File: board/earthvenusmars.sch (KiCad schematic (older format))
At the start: 31 parts, among them J1 Conn_01x05_Female, SW1 SW_SPST, SW2 SW_SPST, U1 ATSAMD21G18A-AU, U2 MIC5504-3.3YM5, Y1 32768Hz

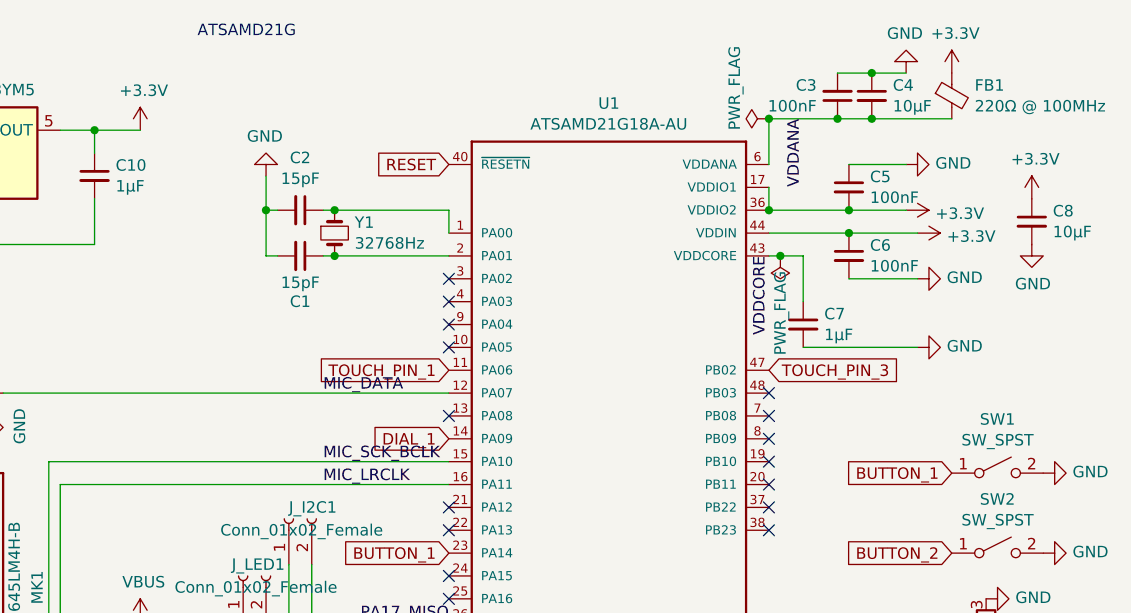
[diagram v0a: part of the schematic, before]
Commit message: add a thermistor that I can use to manage thermals
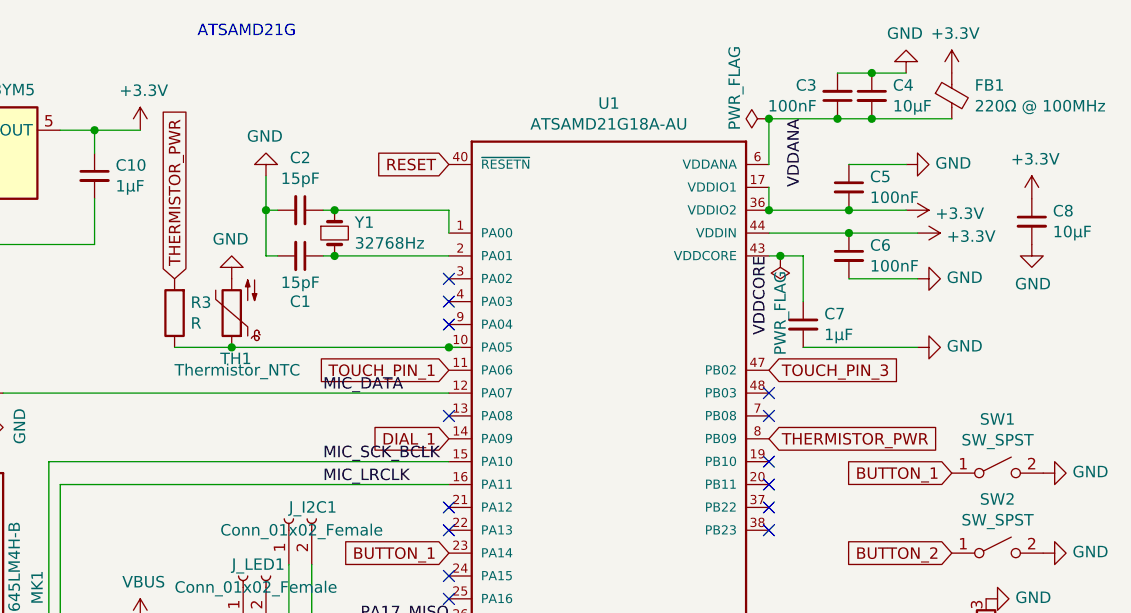
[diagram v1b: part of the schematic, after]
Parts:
- added R3: R, Resistor_SMD:R_0603_1608Metric, symbol Device:R
- added TH1: Thermistor_NTC, Resistor_SMD:R_0603_1608Metric, symbol Device:Thermistor_NTC
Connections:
- net GND: now also TH1.2
- net at U1.10 (PA05): now also R3.1, TH1.1
- net THERMISTOR_PWR: now reaches U1.8 (PB09)
- net THERMISTOR_PWR: now also R3.2
- no-connect marks 21 -> 19
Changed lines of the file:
@@
 NoConn ~ 5350 2350
 NoConn ~ 5350 2450
-NoConn ~ 5350 2550
 NoConn ~ 5350 2650
 NoConn ~ 5350 2750
@@
 Text GLabel 5350 2250 2    50   Input ~ 0
 TOUCH_PIN_3
-NoConn ~ 3950 2150
 $Comp
 L Connector:Conn_01x02_Female J_LED1
@@
 Wire Wire Line
 	2600 4800 3400 4800
+$Comp
+L Device:Thermistor_NTC TH1
+U 1 1 60C6FD5E
+P 3000 2000
+F 0 "TH1" H 3050 2200 50  0000 R CNN
+F 1 "Thermistor_NTC" H 3250 2250 50  0000 R CNN
+F 2 "Resistor_SMD:R_0603_1608Metric" H 3000 2050 50  0001 C CNN
+F 3 "~" H 3000 2050 50  0001 C CNN
+F 4 "ERTJ1VG103GA" H 3000 2000 50  0001 C CNN "Designation"
+	1    3000 2000
+	-1   0    0    1
+$EndComp
+$Comp
+L Device:R R3
+U 1 1 60C7ADC4
+P 2750 2000
+F 0 "R3" H 2680 1954 50  0000 R CNN
+F 1 "R" H 2680 2045 50  0000 R CNN
+F 2 "Resistor_SMD:R_0603_1608Metric" V 2680 2000 50  0001 C CNN
+F 3 "~" H 2750 2000 50  0001 C CNN
+	1    2750 2000
+	-1   0    0    1
+$EndComp
+Text GLabel 5350 2550 2    50   Input ~ 0
+THERMISTOR_PWR
+Text GLabel 2750 1850 1    50   Input ~ 0
+THERMISTOR_PWR
+Wire Wire Line
+	3000 2150 3950 2150
+$Comp
+L power:GND #PWR?
+U 1 1 60C9B9A5
+P 3000 1850
+F 0 "#PWR?" H 3000 1600 50  0001 C CNN
+F 1 "GND" H 3005 1677 50  0000 C CNN
+F 2 "" H 3000 1850 50  0001 C CNN
+F 3 "" H 3000 1850 50  0001 C CNN
+	1    3000 1850
+	-1   0    0    1
+$EndComp
+Connection ~ 3950 2150
+Wire Wire Line
+	3950 2150 4000 2150
+Connection ~ 3000 2150
+Wire Wire Line
+	2750 2150 3000 2150
 $EndSCHEMATC

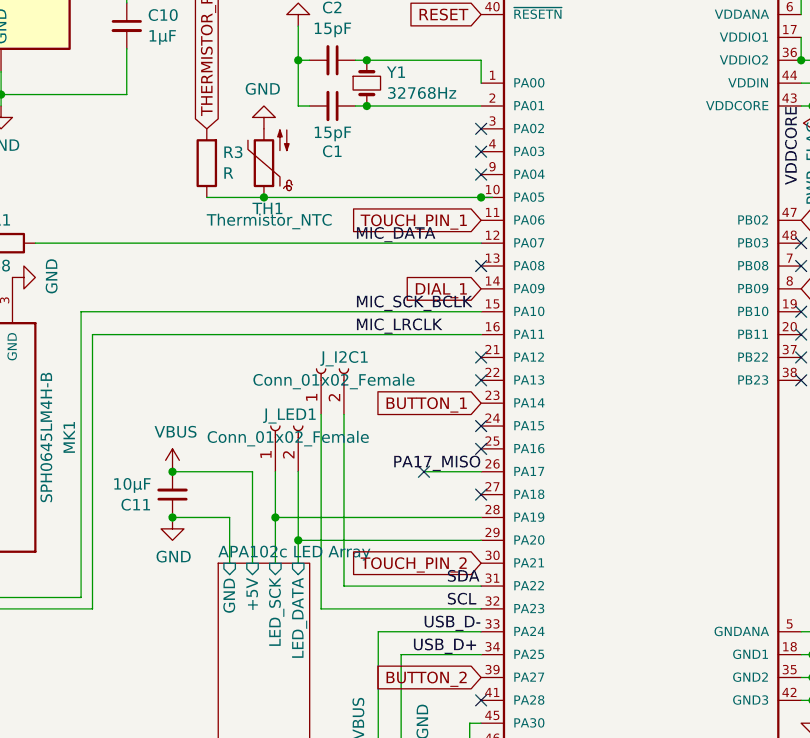
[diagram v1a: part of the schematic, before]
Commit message: move touch pin 2 because AdaFruit_FreeTouch only supports PA02 thru PA07 for self-capacitance; run power to mic and VDDANA on the far side of the VDDIO capacitor to save a via, I think this'll be fine; scoot a bunch of stuff around to optimize ground plane
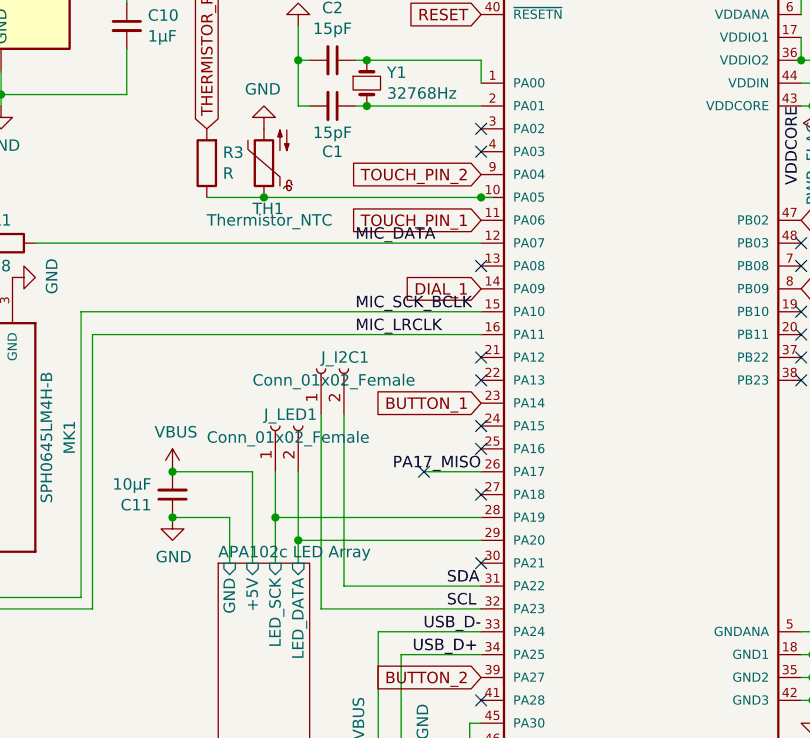
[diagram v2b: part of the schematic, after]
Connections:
- net TOUCH_PIN_2: now also U1.9 (PA04); no longer U1.30 (PA21)
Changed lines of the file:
@@
 NoConn ~ 3950 2950
 NoConn ~ 3950 2850
-NoConn ~ 3950 2050
+NoConn ~ 3950 2450
 NoConn ~ 3950 1950
 NoConn ~ 3950 1850
@@
 Text GLabel 3950 2250 0    50   Input ~ 0
 TOUCH_PIN_1
-NoConn ~ 3950 2450
-Text GLabel 3950 3750 0    50   Input ~ 0
+NoConn ~ 3950 3750
+Text GLabel 3950 2050 0    50   Input ~ 0
 TOUCH_PIN_2
 Text GLabel 6300 3950 0    50   Input ~ 0
@@
 	3000 2150 3950 2150
 $Comp
-L power:GND #PWR?
+L power:GND #PWR0137
 U 1 1 60C9B9A5
 P 3000 1850
-F 0 "#PWR?" H 3000 1600 50  0001 C CNN
+F 0 "#PWR0137" H 3000 1600 50  0001 C CNN
 F 1 "GND" H 3005 1677 50  0000 C CNN
 F 2 "" H 3000 1850 50  0001 C CNN

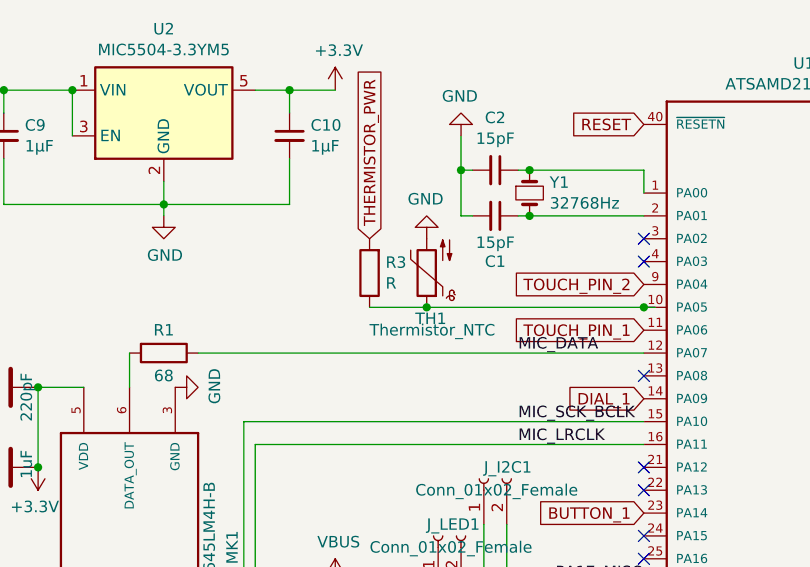
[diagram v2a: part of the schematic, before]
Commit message: thermistor series resister marked as 10k
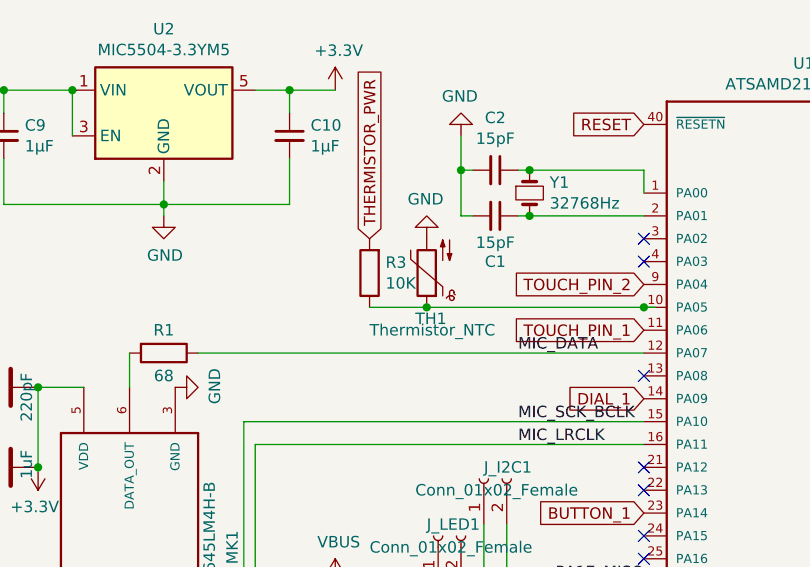
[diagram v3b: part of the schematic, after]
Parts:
- R3: value R -> 10K
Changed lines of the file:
@@
 P 2750 2000
 F 0 "R3" H 2680 1954 50  0000 R CNN
-F 1 "R" H 2680 2045 50  0000 R CNN
+F 1 "10K" H 2680 2045 50  0000 R CNN
 F 2 "Resistor_SMD:R_0603_1608Metric" V 2680 2000 50  0001 C CNN
 F 3 "~" H 2750 2000 50  0001 C CNN

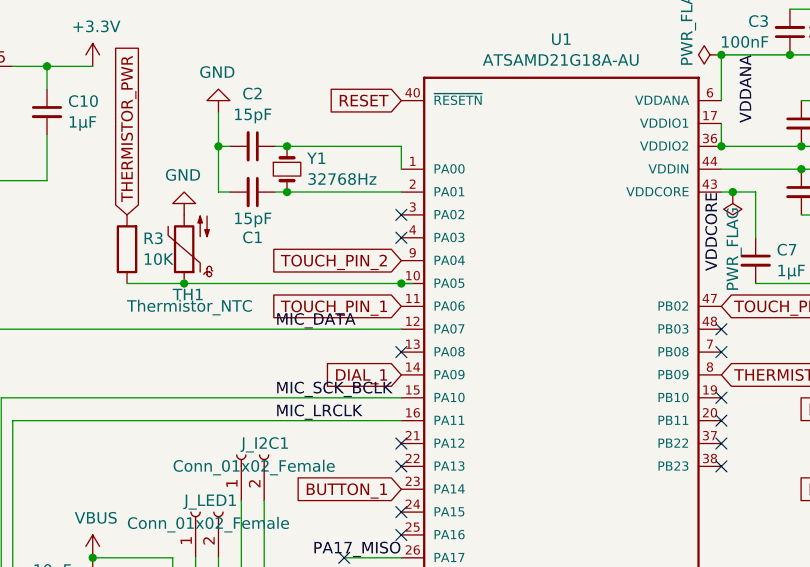
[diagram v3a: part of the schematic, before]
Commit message: add support for thermistor reads with a custom analogRead function that restores settings needed by the ADC interrupt-driven brightness dial; scale brightness down as temperature increases (partially tested); schematic tweak was redundant wire
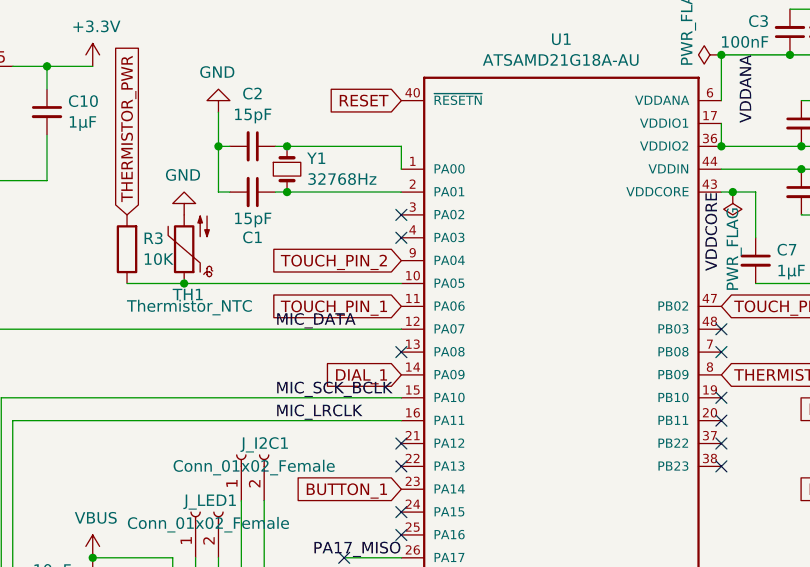
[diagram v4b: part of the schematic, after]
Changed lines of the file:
@@
 	-1   0    0    1
 $EndComp
-Connection ~ 3950 2150
-Wire Wire Line
-	3950 2150 4000 2150
 Connection ~ 3000 2150
 Wire Wire Line

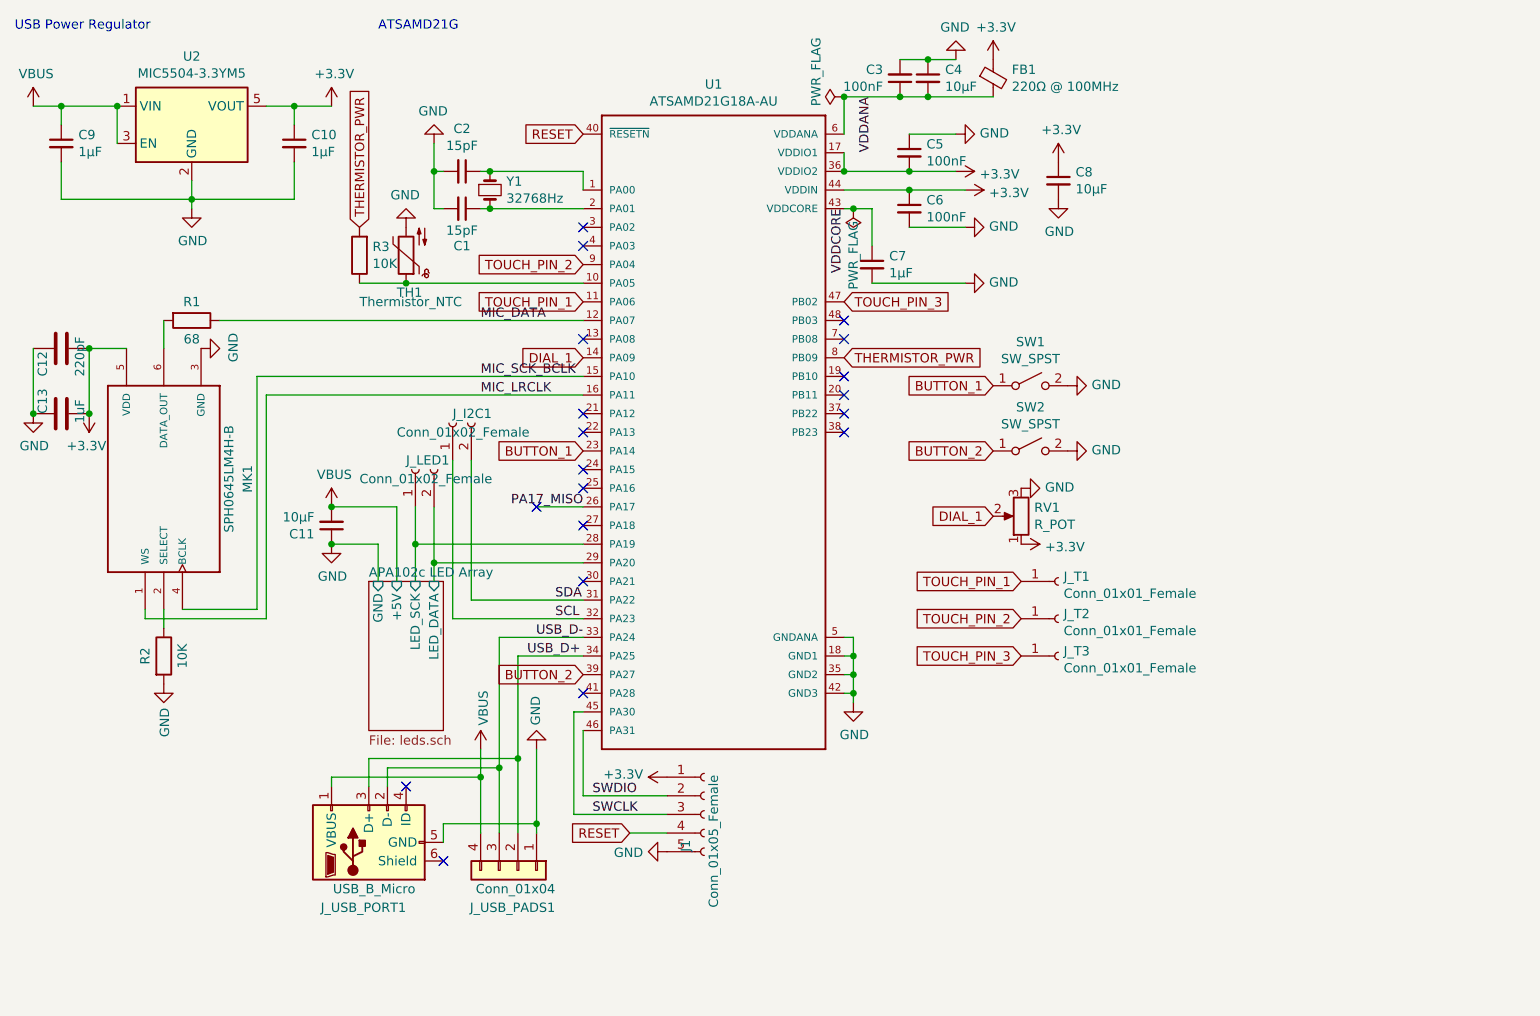
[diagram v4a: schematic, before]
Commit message: change µ to u in micro-faraday labels for consistency and cause it's easier to search for and everyone understands it
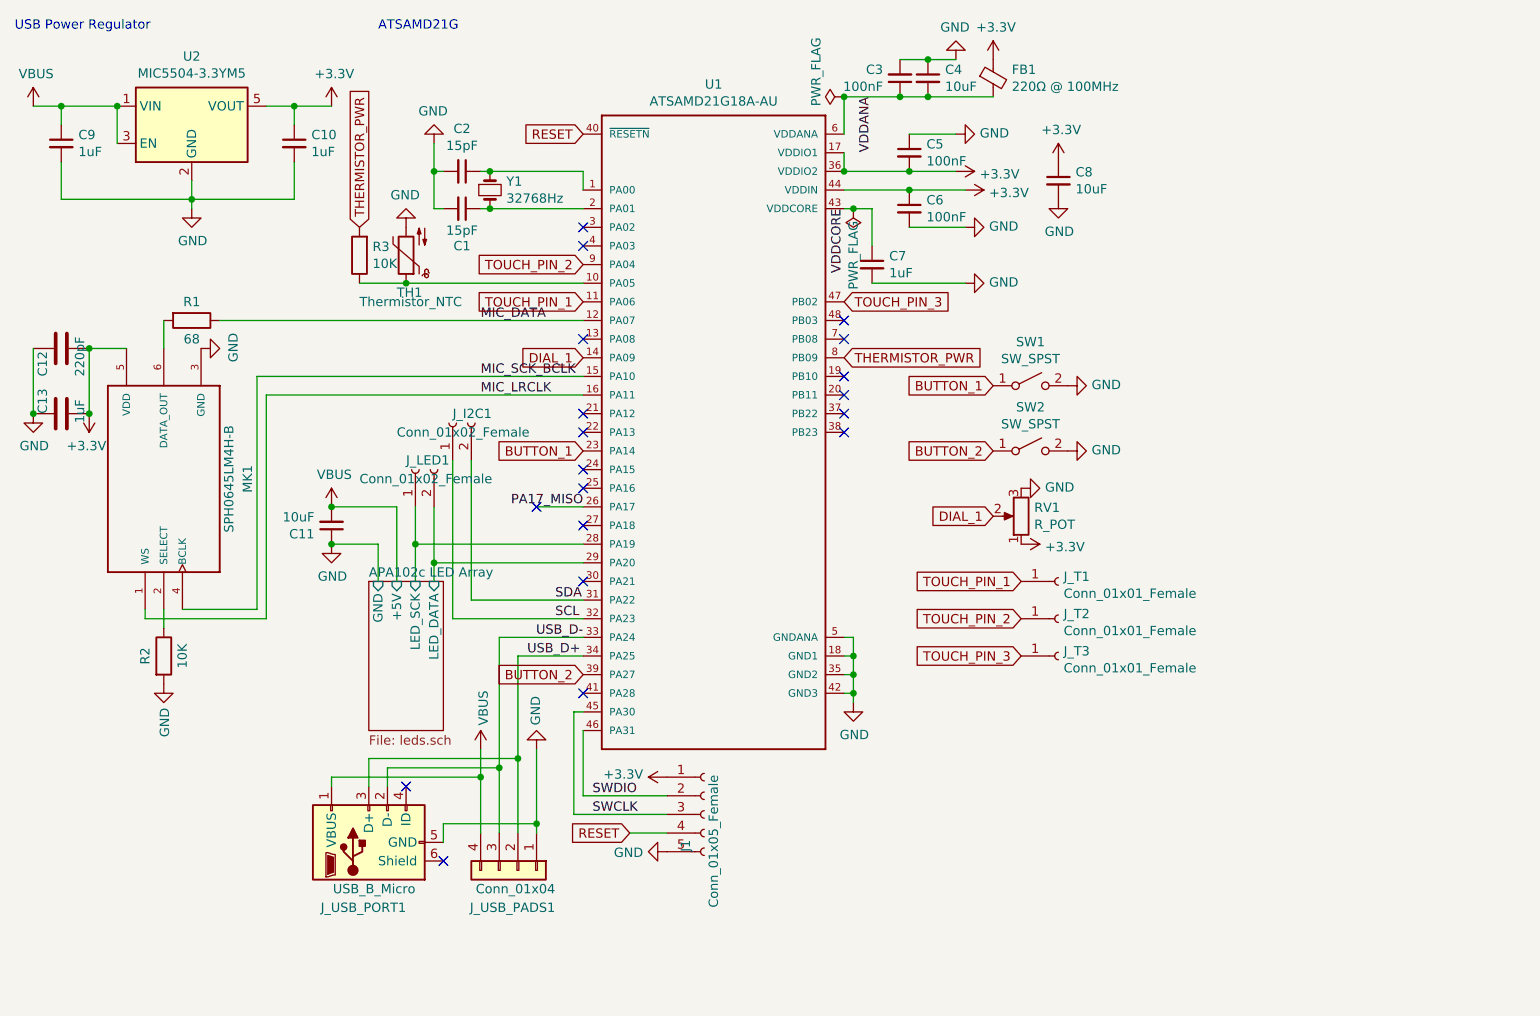
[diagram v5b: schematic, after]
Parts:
- C10, C7, C9: value 1µF -> 1uF
- C11, C4, C8: value 10µF -> 10uF
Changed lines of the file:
@@
 P 5800 1050
 F 0 "C4" H 5892 1096 50  0000 L CNN
-F 1 "10µF" H 5892 1005 50  0000 L CNN
+F 1 "10uF" H 5892 1005 50  0000 L CNN
 F 2 "Capacitor_SMD:C_0402_1005Metric" H 5800 1050 50  0001 C CNN
 F 3 "~" H 5800 1050 50  0001 C CNN
@@
 P 5500 2050
 F 0 "C7" H 5408 2096 50  0000 R CNN
-F 1 "1µF" H 5408 2005 50  0000 R CNN
+F 1 "1uF" H 5408 2005 50  0000 R CNN
 F 2 "Capacitor_SMD:C_0603_1608Metric" H 5500 2050 50  0001 C CNN
 F 3 "~" H 5500 2050 50  0001 C CNN
@@
 P 6500 1600
 F 0 "C8" H 6408 1646 50  0000 R CNN
-F 1 "10µF" H 6408 1555 50  0000 R CNN
+F 1 "10uF" H 6408 1555 50  0000 R CNN
 F 2 "Capacitor_SMD:C_0402_1005Metric" H 6500 1600 50  0001 C CNN
 F 3 "~" H 6500 1600 50  0001 C CNN
@@
 P 1150 1400
 F 0 "C9" H 1058 1446 50  0000 R CNN
-F 1 "1µF" H 1058 1355 50  0000 R CNN
+F 1 "1uF" H 1058 1355 50  0000 R CNN
 F 2 "Capacitor_SMD:C_0603_1608Metric" H 1150 1400 50  0001 C CNN
 F 3 "~" H 1150 1400 50  0001 C CNN
@@
 P 2400 1400
 F 0 "C10" H 2308 1446 50  0000 R CNN
-F 1 "1µF" H 2308 1355 50  0000 R CNN
+F 1 "1uF" H 2308 1355 50  0000 R CNN
 F 2 "Capacitor_SMD:C_0603_1608Metric" H 2400 1400 50  0001 C CNN
 F 3 "~" H 2400 1400 50  0001 C CNN
@@
 P 2600 3450
 F 0 "C11" H 2508 3496 50  0000 R CNN
-F 1 "10µF" H 2508 3405 50  0000 R CNN
+F 1 "10uF" H 2508 3405 50  0000 R CNN
 F 2 "Capacitor_SMD:C_0402_1005Metric" H 2600 3450 50  0001 C CNN
 F 3 "~" H 2600 3450 50  0001 C CNN
